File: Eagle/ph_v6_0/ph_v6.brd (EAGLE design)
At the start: 100 x 84.6 mm, 177 parts, among them CON1 JACK_DC_BARREL, IC1 MCP1703DB, IC2 TL084D, IC3 TL084D, IC4 DRV8811, IC5 TPS60400DBV, IC6 DRV8811, J1 RJ12RIGHTANGLE-I2C, J2 RJ12RIGHTANGLE-I2C, U1 HX711, U100 RN2483, X2 8MHz, X3 FH12-08S-1SH, X4 MINI-USB

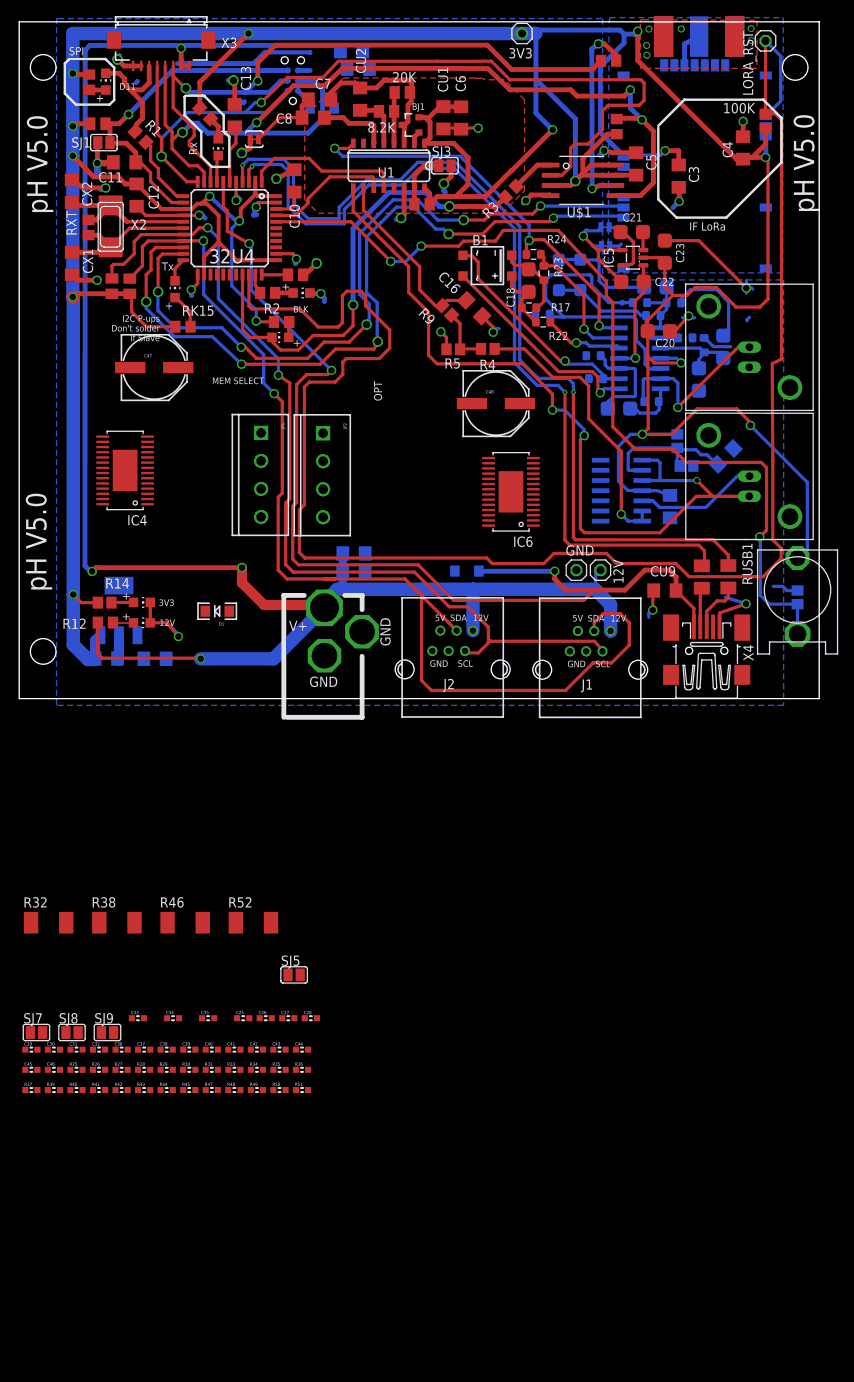
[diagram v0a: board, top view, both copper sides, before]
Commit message: Progress on pH board v6_0 with DRV8811
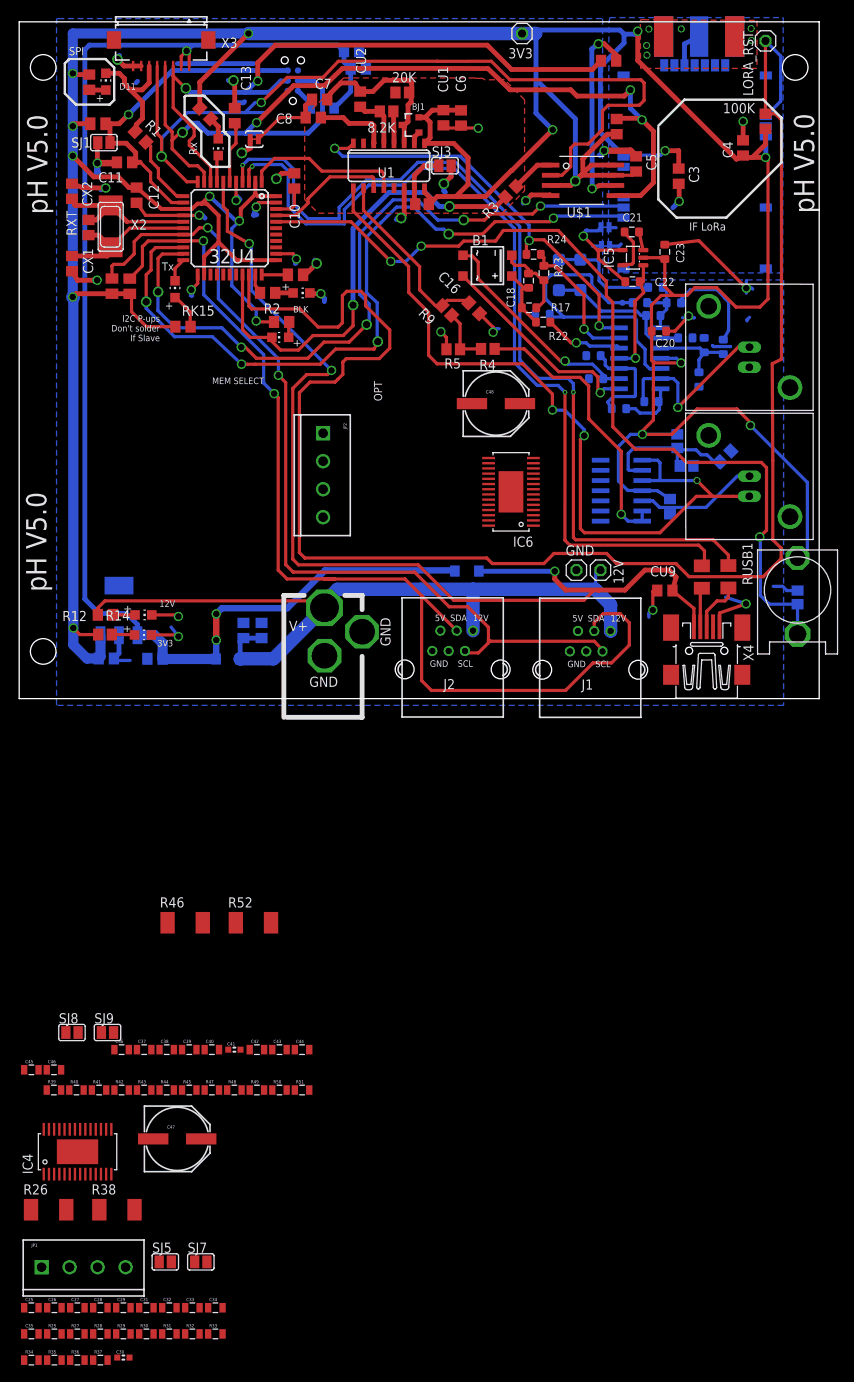
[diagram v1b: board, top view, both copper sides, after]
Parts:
- 20K, 8.2K, RK5: device resistor:M0805 -> resistor:R0805
- C1, C10, C11, C12, C13, C14, C15, C16, C2, C3, C4, C5, C6, C7, C8, CU1, CU2, CU3, CU4, CU7, CU8, CU9, CX1, CX2: device rcl:C1206 -> rcl:C0805
- C17, C18, C19, C20, C21, C22, C23, C24, C9: device SparkysWidgets:1206 -> SparkysWidgets:0805
- C25, C26, C27, C28, C29, C31, C32, C36, C37, C38, C39, C40, C42, C43, C44, C45, C46, R27, R28, R37, R39, R40, R41, R42, R43, R44, R45, R47, R48, R49, R50, R51: device freetronics-master-v1:0603 -> freetronics-master-v1:0805
- C33: value 100nF 0603 -> 100nF; device freetronics-master-v1:0603 -> freetronics-master-v1:0805
- C34, C35: value 220nF 0603 -> 220nF; device freetronics-master-v1:0603 -> freetronics-master-v1:0805
- R25: value 3K3 -> 47K; device freetronics-master-v1:0603 -> freetronics-master-v1:0805
- R26: value 47K -> 0.2R 1W; device freetronics-master-v1:0603 -> rcl:R2010
- R29: value 10K -> 3k3; device freetronics-master-v1:0603 -> freetronics-master-v1:0805
- R30, R31, R33, R34, R35, R36: value 10K -> 10k; device freetronics-master-v1:0603 -> freetronics-master-v1:0805
- R32: value 0.2R 1W -> 10k; device rcl:R2010 -> freetronics-master-v1:0805
- moved JP1 107.8 mm to (-2.20, -74.0), turned to 0 degrees
- moved C47 96.5 mm to (14.8, -57.9)
- moved IC4 85.4 mm to (2.29, -59.5), turned to 0 degrees
- moved R32 54.4 mm to (16.6, -82.3)
- moved R34 46.0 mm to (-3.48, -85.6)
- moved R35 45.9 mm to (-0.60, -85.6)
- moved R36 45.9 mm to (2.27, -85.6)
- moved C35 45.2 mm to (-3.48, -82.3)
- moved C25 44.8 mm to (-3.48, -79.0)
- moved C26 44.8 mm to (-0.60, -79.0)
- moved C27 44.8 mm to (2.27, -79.0)
- moved C28 44.7 mm to (5.15, -79.0)
- moved C30 39.5 mm to (8.02, -85.3)
- moved SJ5 39.3 mm to (13.3, -73.3)
- moved C33 36.8 mm to (16.6, -79.0)
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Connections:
- removed net D2: IC4.3
- removed net D5: IC4.19
- removed net N$62: C30.1, IC4.14, R32.2
- removed net N$63: C28.1, IC4.5, R29.1, R37.2
- removed net N$64: C25.1, IC4.6, R26.2
- removed net N$68: C27.1, IC4.8, R25.1, R28.2
- removed net N$70: IC4.12, R30.1, SJ5.2
- removed net N$71: IC4.13, R31.1, SJ7.2
- new net N$13: C30.1, IC4.14, R26.2
- new net N$14: C28.1, IC4.5, R30.1, R37.2
- new net N$15: C25.1, IC4.6, R25.2
- new net N$32: C27.1, IC4.8, R28.2, R29.1
- new net N$37: IC4.12, R31.1, SJ5.2
- new net N$53: IC4.13, R32.1, SJ7.2
- net +12V: no longer X3.1, X3.2
- net 3.3V: now also R32.2; no longer R25.2
- net D3: now also IC4.3
- net D6: now also IC4.19
- net GND: now also R25.1; no longer R32.1
- net VDD: now also X3.1, X3.2
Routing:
- net VDD: track 0.00 -> 174.2 mm, vias 0 -> 3
- net +12V: track 223.5 -> 98.3 mm, vias 4 -> 0
- net GND: track 173.0 -> 167.1 mm, vias 27 -> 28
- net N$39: track 6.39 -> 4.17 mm
- net RESET: track 42.3 -> 43.6 mm
- net 3.3V: track 536.0 -> 537.0 mm
- net LGND: track 15.8 -> 16.8 mm
- net ANGND: track 7.38 -> 8.25 mm
- net N$49: track 8.58 -> 7.81 mm
- net N$5: track 21.2 -> 21.9 mm
- net SCL: track 112.3 -> 111.7 mm
- net N$44: track 13.5 -> 14.0 mm
- net N$36: track 6.79 -> 7.29 mm

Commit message: progress on phv6, mem select now on A3, LoRa reset on A1, Stepper 1(PWM D9, dir D8), Stepper 2(PWM D10, dir D5)
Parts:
- removed JP2: (no value), freetronics-master-v1:SCREWTERMINAL-3.5MM-4
- added JP3: (no value), jumper:JP4
- JP1: device freetronics-master-v1:SCREWTERMINAL-3.5MM-4 -> jumper:JP4
- moved JP1 104.4 mm to (33.1, 24.3), turned to 90 degrees
- moved C47 96.6 mm to (44.3, 34.1)
- moved IC4 94.3 mm to (46.0, 24.1), turned to 270 degrees
- moved C48 44.0 mm to (10.6, 34.9)
- moved IC6 41.9 mm to (14.6, 24.3)
- moved LDMEM 41.0 mm to (61.1, 66.1)
- moved RK19 41.0 mm to (61.2, 68.0)
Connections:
- removed net D3: IC4.3, IC6.3
- removed net D6: IC4.19, IC6.19
- net A1: now also 100K.2, LORA_RST.1, U100.P$32
- net A3: now also LDMEM.C, R3.2
- net D10*: now also IC6.19; no longer LDMEM.C, R3.2
- net D5*: now also IC6.3; no longer 100K.2, LORA_RST.1, U100.P$32
- net D8*: now also IC4.3
- net D9*: now also IC4.19
- net N$2: now also JP1.4; no longer JP1.1
- net N$4: now also JP1.2; no longer JP1.3
- net N$55: now also JP1.1; no longer JP1.4
- net N$56: now also JP1.3; no longer JP1.2
- net N$73: now also JP3.4; no longer JP2.1
- net N$74: now also JP3.2; no longer JP2.3
- net N$95: now also JP3.1; no longer JP2.4
- net N$96: now also JP3.3; no longer JP2.2
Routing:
- net D5*: track 207.8 -> 3.94 mm
- net A1: track 0.00 -> 173.5 mm
- net D10*: track 57.8 -> 8.25 mm, vias 2 -> 0
- net A3: track 0.00 -> 42.2 mm, vias 0 -> 2
- net 3.3V: track 537.0 -> 516.2 mm, vias 17 -> 16
- net GND: track 167.1 -> 168.9 mm

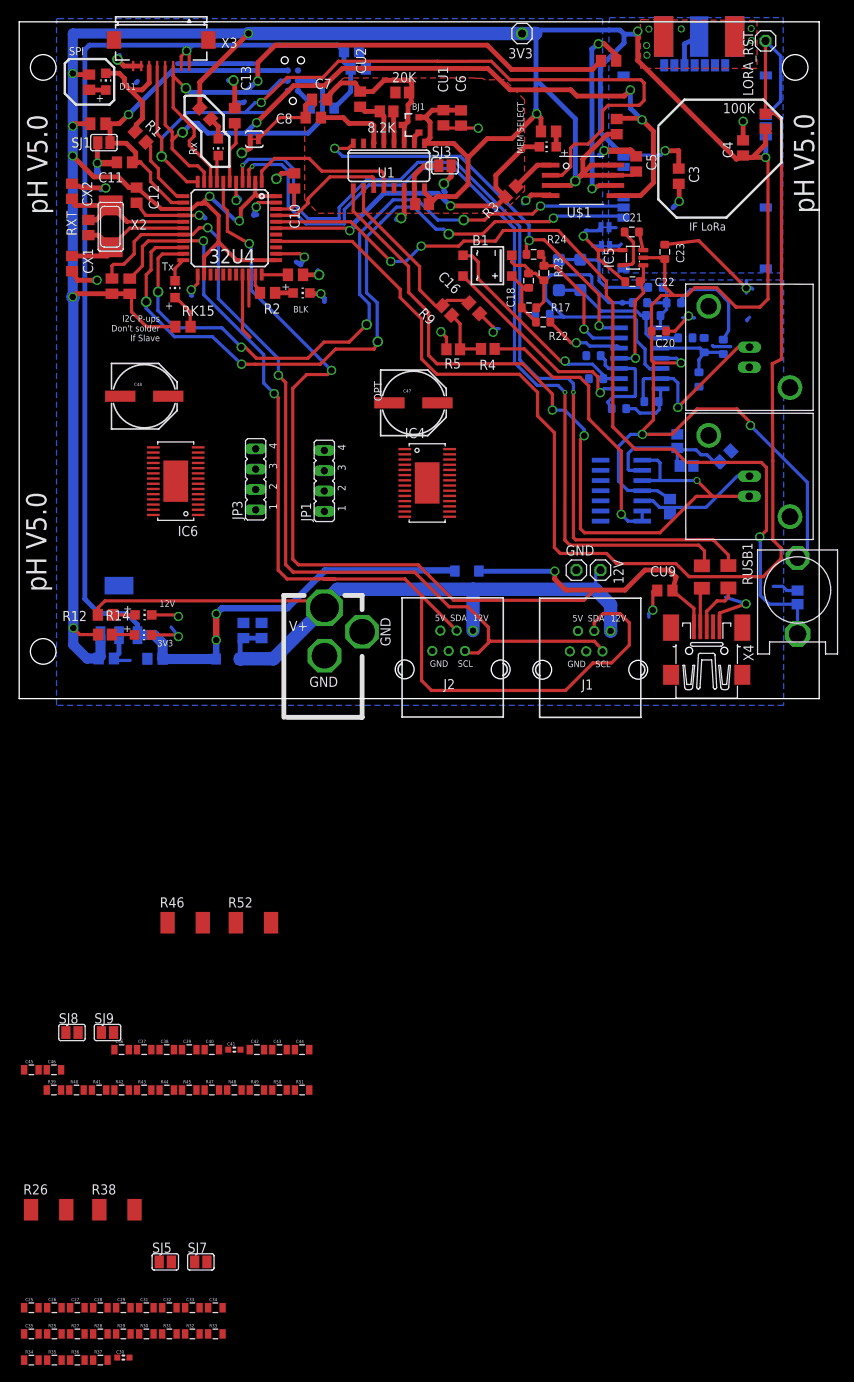
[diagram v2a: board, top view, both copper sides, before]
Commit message: shortened boards by 1mm, closes #68
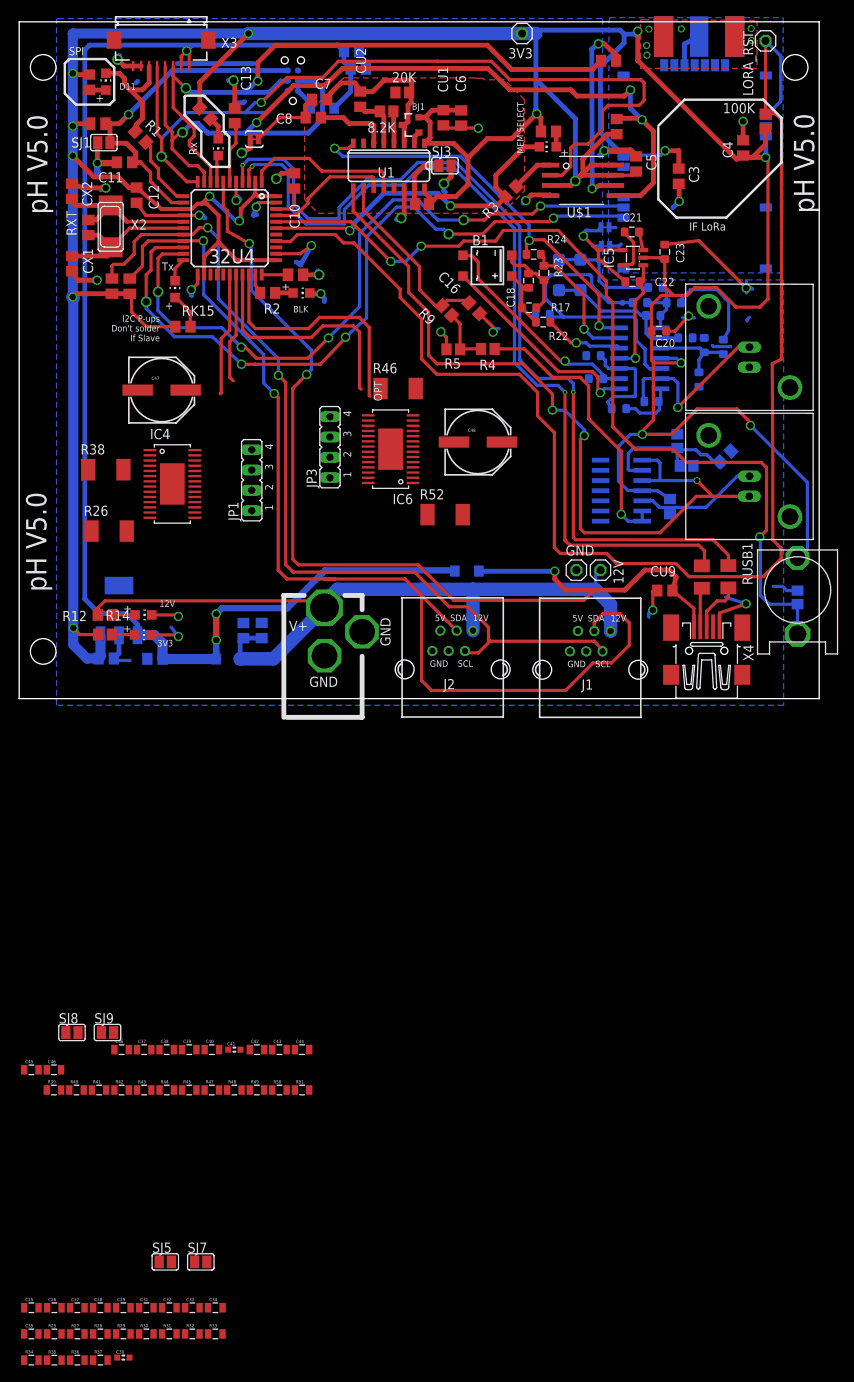
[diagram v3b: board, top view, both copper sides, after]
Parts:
- moved R38 92.5 mm to (5.83, 25.7)
- moved R26 85.2 mm to (6.24, 18.0)
- moved R46 71.9 mm to (42.4, 35.9)
- moved R52 56.4 mm to (48.2, 20.1)
- moved C48 42.1 mm to (52.3, 29.2)
- moved IC4 31.9 mm to (14.1, 23.9)
- moved C47 31.5 mm to (12.8, 35.7)
- moved IC6 27.2 mm to (41.4, 28.3)
- moved JP3 10.1 mm to (33.8, 28.5)
- moved JP1 9.07 mm to (24.1, 24.4)
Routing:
- net D5*: track 3.94 -> 31.0 mm
- net D10*: track 8.25 -> 30.1 mm
- net D8*: track 0.00 -> 15.4 mm
- net D9*: track 0.00 -> 13.8 mm
- net RX: track 94.5 -> 90.6 mm
- net VUSB: track 132.7 -> 129.1 mm
- net TX: track 89.0 -> 86.2 mm
- net GND: track 168.9 -> 171.6 mm
- net A1: track 173.5 -> 174.2 mm

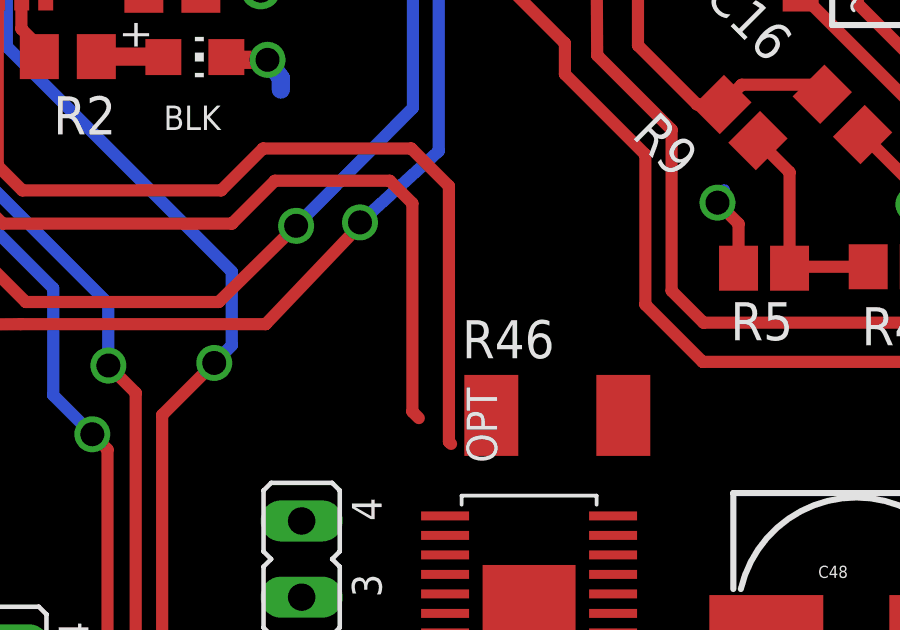
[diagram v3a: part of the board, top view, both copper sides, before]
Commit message: added protection resistor, closes #74
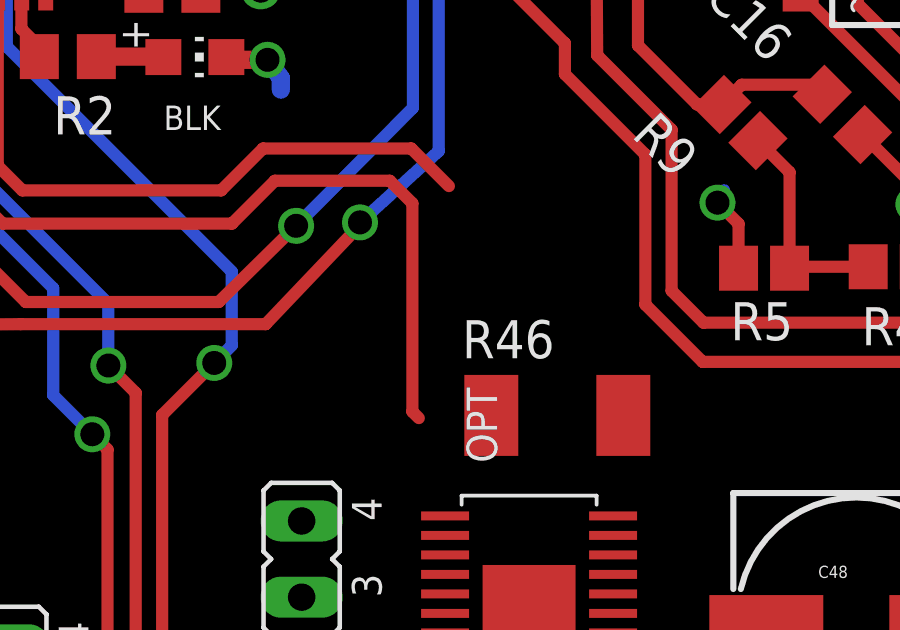
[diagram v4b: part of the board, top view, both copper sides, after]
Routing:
- net D5*: track 31.0 -> 22.4 mm
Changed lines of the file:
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@@
 <layer number="23" name="tOrigins" color="15" fill="1" visible="yes" active="yes"/>
 <layer number="24" name="bOrigins" color="15" fill="1" visible="yes" active="yes"/>
-<layer number="25" name="tNames" color="7" fill="1" visible="yes" active="yes"/>
-<layer number="26" name="bNames" color="7" fill="1" visible="yes" active="yes"/>
-<layer number="27" name="tValues" color="7" fill="1" visible="no" active="yes"/>
-<layer number="28" name="bValues" color="7" fill="1" visible="no" active="yes"/>
+<layer number="25" name="tNames" color="7" fill="1" visible="no" active="yes"/>
+<layer number="26" name="bNames" color="7" fill="1" visible="no" active="yes"/>
+<layer number="27" name="tValues" color="7" fill="1" visible="yes" active="yes"/>
+<layer number="28" name="bValues" color="7" fill="1" visible="yes" active="yes"/>
 <layer number="29" name="tStop" color="7" fill="3" visible="no" active="yes"/>
 <layer number="30" name="bStop" color="7" fill="6" visible="no" active="yes"/>
@@
 <wire x1="32.558328125" y1="44.756740625" x2="37.501609375" y2="44.756740625" width="0.4064" layer="1"/>
 <wire x1="37.501609375" y1="44.756740625" x2="38.754796875" y2="43.503553125" width="0.4064" layer="1"/>
-<wire x1="38.754796875" y1="43.503553125" x2="38.754796875" y2="34.98189375" width="0.4064" layer="1"/>
-<wire x1="38.754796875" y1="34.98189375" x2="38.82643125" y2="34.910259375" width="0.4064" layer="1"/>
-<wire x1="38.82643125" y1="34.910259375" x2="44.22649375" y2="25.359559375" width="0" layer="19" extent="1-1"/>
+<wire x1="38.754796875" y1="43.503553125" x2="44.22649375" y2="25.359559375" width="0" layer="19" extent="1-1"/>
 </signal>
 <signal name="VUSB">
